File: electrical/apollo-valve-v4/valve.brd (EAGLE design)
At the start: 160 x 100 mm, 80 parts, among them J1 VALVE2, J2 VALVE1, J4 S1, J5 S2, U1 DRV8806-SSOP, U2 DRV8806-SSOP, U3 TPS54202, U4 DRV8806-SSOP, U5 DRV8806-SSOP, U6 TPS54202

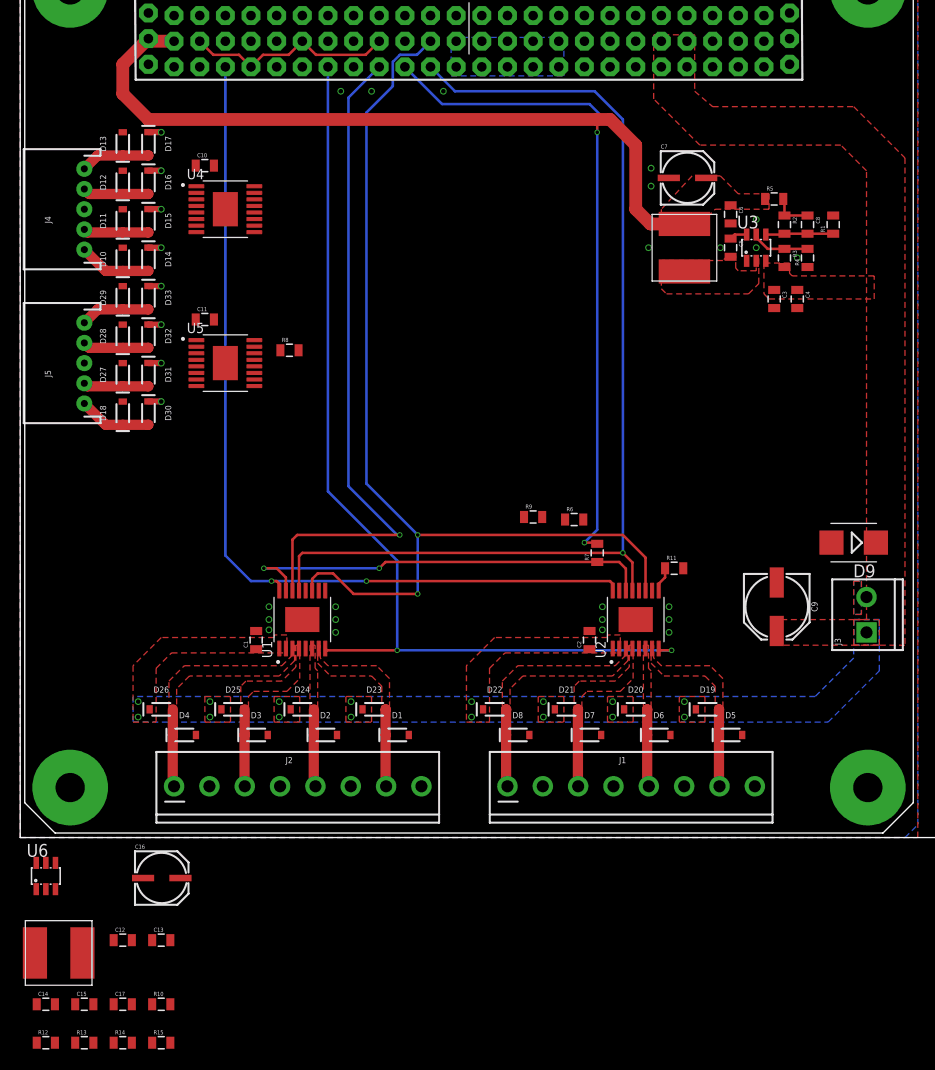
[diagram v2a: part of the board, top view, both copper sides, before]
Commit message: First layout pass for complete valve board
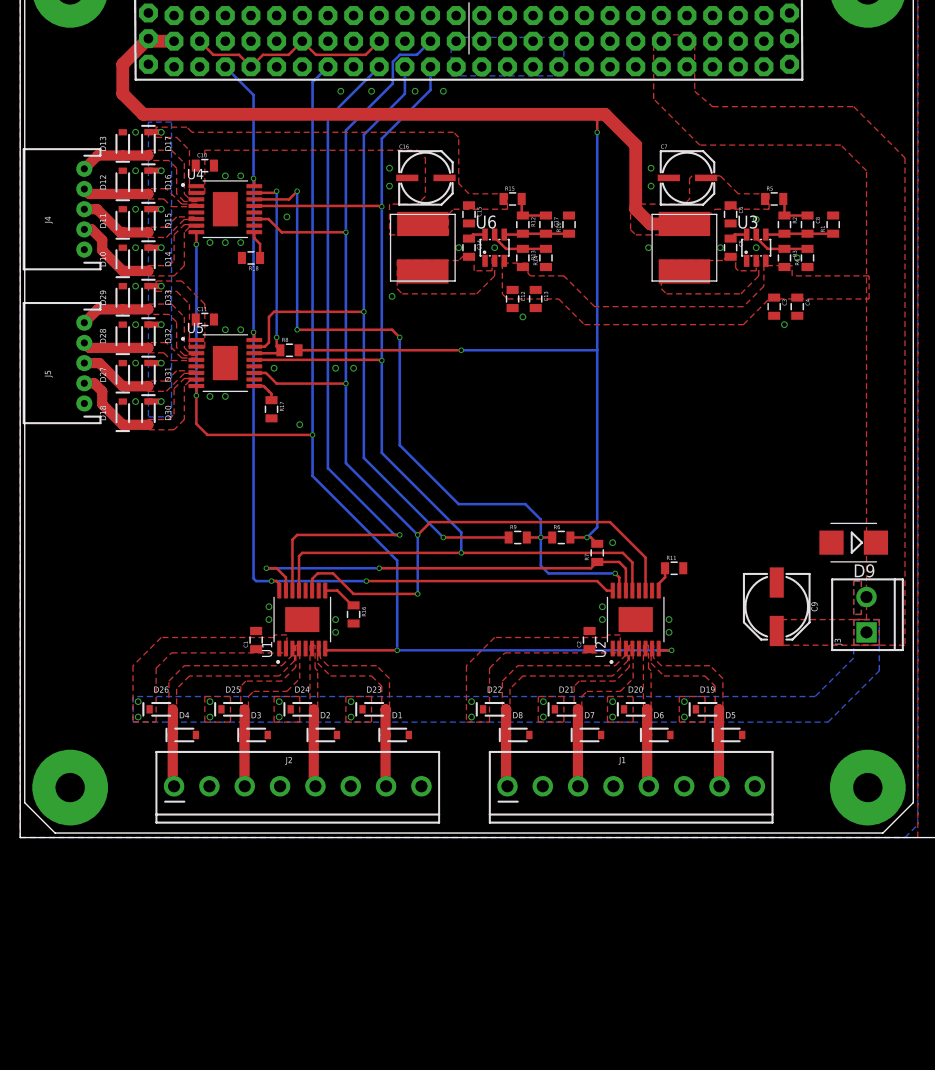
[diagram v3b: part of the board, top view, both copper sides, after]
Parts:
- added R16, R17, R18: 2.2K, apollo-ctrl-v4:0805
- moved R12 93.8 mm to (49.8, 60.7), turned to 270 degrees
- moved R15 90.5 mm to (48.8, 63.2)
- moved R13 89.0 mm to (49.8, 57.4), turned to 270 degrees
- moved R14 88.3 mm to (52.1, 57.4), turned to 90 degrees
- moved C17 87.9 mm to (52.1, 60.7), turned to 270 degrees
- moved R10 87.1 mm to (54.4, 60.7), turned to 90 degrees
- moved C15 87.0 mm to (44.5, 61.7), turned to 270 degrees
- moved C14 85.9 mm to (44.5, 58.4), turned to 270 degrees
- moved L2 78.6 mm to (39.9, 58.4), turned to 90 degrees
- moved U6 76.5 mm to (47.0, 58.4)
- moved C12 74.3 mm to (48.8, 53.3), turned to 270 degrees
- moved C16 74.1 mm to (40.1, 65.5)
- moved C13 73.5 mm to (51.1, 53.3), turned to 270 degrees
- moved R9 2.54 mm to (49.3, 29.7)
- moved R6 2.18 mm to (53.6, 29.7)
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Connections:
- removed net RESET: R11.1, U1.9, U2.9, U4.9, U5.9
- new net R1: R11.1, U2.9
- new net R2: R16.1, U1.9
- new net R3: R17.1, U5.9
- new net R4: R18.1, U4.9
- net GND: now also J4.1, J5.1, R16.2, R17.2, R18.2; no longer J4.3, J5.3
- net S1C: now also J4.3; no longer J4.2
- net S1D: now also J4.2; no longer J4.1
- net S2C: now also J5.3; no longer J5.2
- net S2D: now also J5.2; no longer J5.1
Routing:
- net CIDO2: track 0.00 -> 73.1 mm, vias 0 -> 5
- net CIDO: track 22.7 -> 71.8 mm, vias 0 -> 2
- net !LOE!: track 96.4 -> 129.5 mm, vias 2 -> 5
- net +5V: track 117.6 -> 148.7 mm, vias 2 -> 3
- net CS1: track 99.9 -> 121.8 mm, vias 2 -> 4
- net CIDO3: track 0.00 -> 20.9 mm, vias 0 -> 2
- net SCK: track 103.9 -> 118.4 mm, vias 1 -> 3
- net FB2: track 0.00 -> 6.45 mm
- net VEN2: track 0.00 -> 5.83 mm
- net FF2: track 0.00 -> 3.97 mm
- net R2: track 0.00 -> 3.41 mm
- net R4: track 0.00 -> 2.79 mm
- net R3: track 0.00 -> 2.65 mm
- net RESET: track 2.47 -> 0.00 mm
- net R1: track 0.00 -> 2.47 mm
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- added copper zone on layer 1, net +12V
- added copper zone on layer 16, net +12V
- added copper zone on layer 1, net S1A
- added copper zone on layer 1, net S1B
- added copper zone on layer 1, net S1C
- added copper zone on layer 1, net S1D
- added copper zone on layer 1, net S2A
- added copper zone on layer 1, net S2B
- added copper zone on layer 1, net S2C
- added copper zone on layer 1, net S2D
- added copper zone on layer 1, net SW2

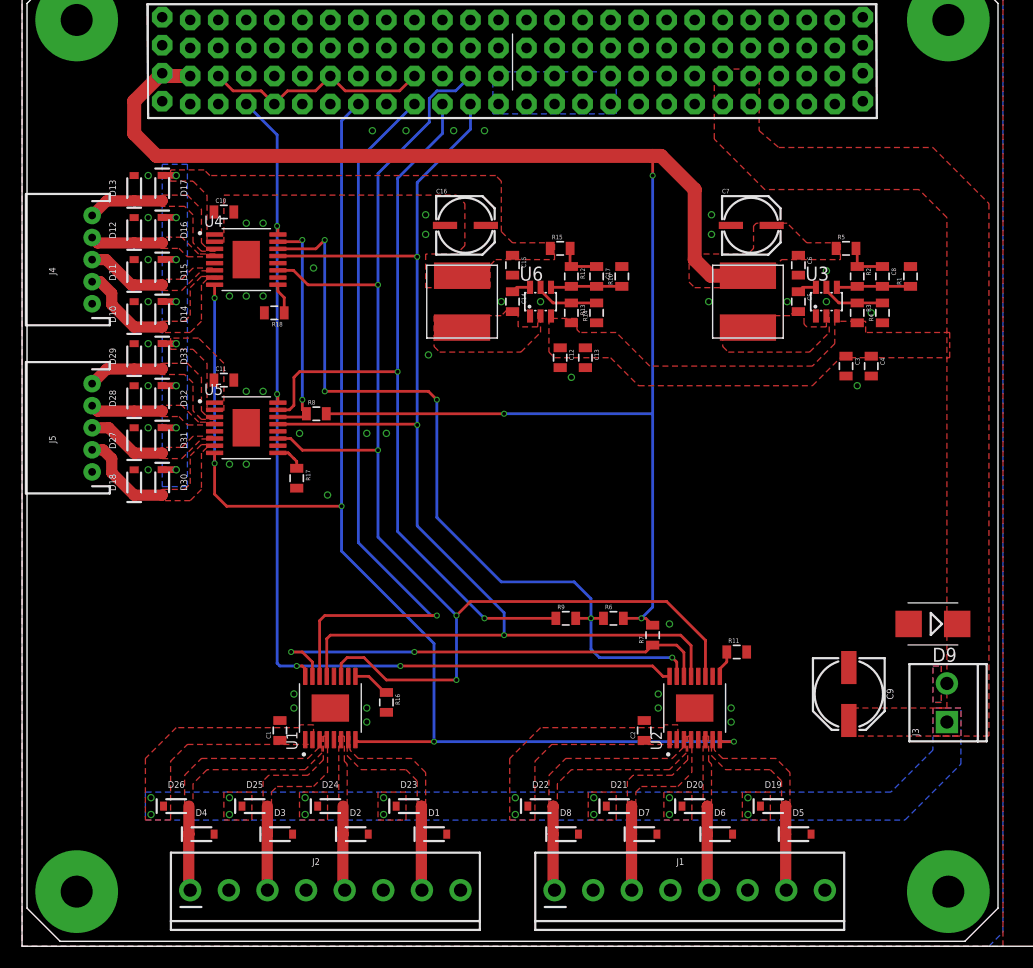
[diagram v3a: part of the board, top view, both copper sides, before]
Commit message: Clean up valve board silkscreen and change diodes to SOD-123
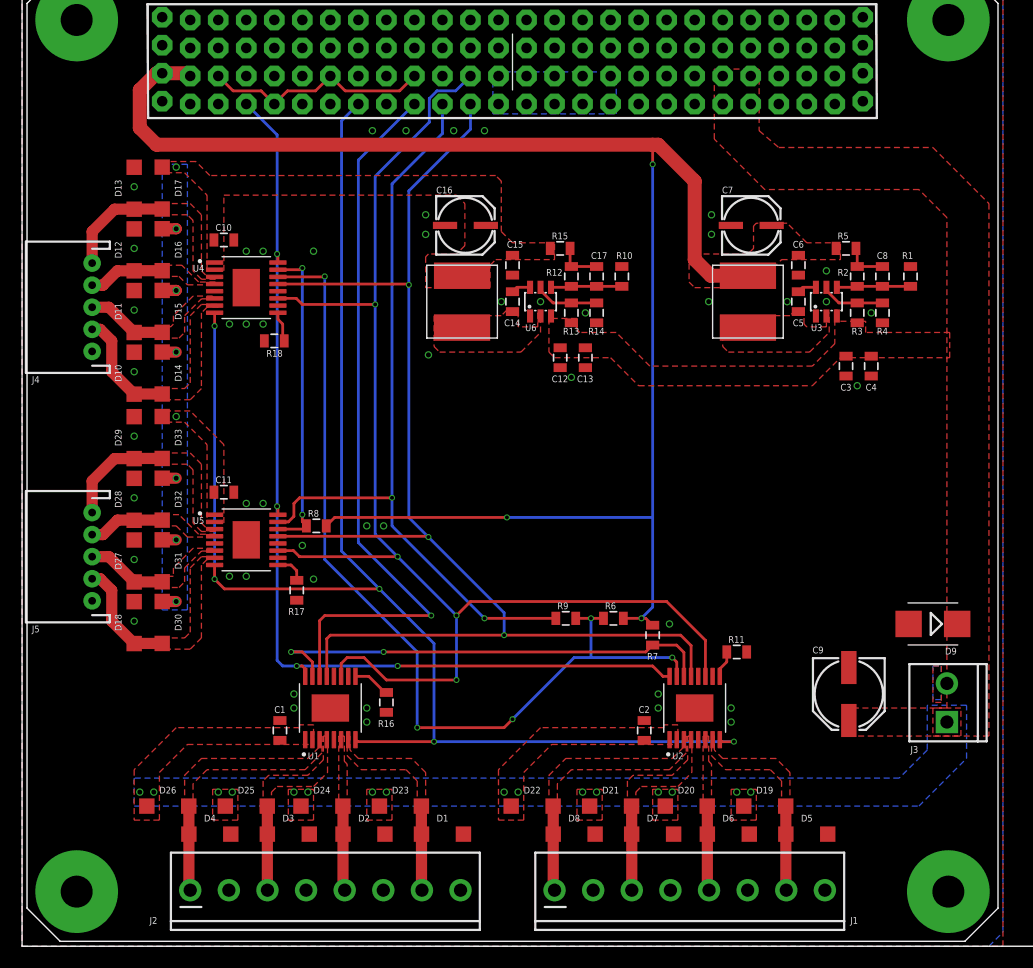
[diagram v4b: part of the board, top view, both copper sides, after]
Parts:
- D1, D10, D11, D12, D13, D14, D15, D16, D17, D18, D19, D2, D20, D21, D22, D23, D24, D25, D26, D27, D28, D29, D3, D30, D31, D32, D33, D4, D5, D6, D7, D8: value BAT46 -> B5819W; device SparkFun-DiscreteSemi:SOD-323 -> diode:SOD123
- moved D18 12.7 mm to (10.2, 29.3)
- moved D30 12.7 mm to (12.7, 29.3)
- moved J5 11.7 mm to (6.35, 35.3)
- moved D27 10.9 mm to (10.2, 34.9)
- moved D31 10.9 mm to (12.7, 34.9)
- moved U5 10.2 mm to (20.3, 36.8)
- moved C11 10.2 mm to (18.3, 41.1)
- moved R17 10.2 mm to (24.9, 32.3)
- moved R8 10.2 mm to (26.7, 38.1)
- moved D28 9.14 mm to (10.2, 40.5)
- moved D32 9.14 mm to (12.7, 40.5)
- moved D29 7.37 mm to (10.2, 46.1)
- moved D33 7.37 mm to (12.7, 46.1)
- moved D10 5.33 mm to (10.2, 51.9)
- moved D14 5.33 mm to (12.7, 52.0)
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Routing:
- net CIDO2: track 73.1 -> 82.3 mm
- net !LOE!: track 129.5 -> 138.3 mm
- net CIDO3: track 20.9 -> 28.5 mm
- net S2A: track 6.90 -> 10.1 mm
- net S1A: track 6.90 -> 10.1 mm
- net +12V: track 10.2 -> 7.63 mm
- net S1D: track 8.66 -> 10.4 mm
- net S2D: track 8.81 -> 10.4 mm
- net CIDO: track 71.8 -> 70.4 mm
- net CS1: track 121.8 -> 123.0 mm
- net +5V: track 148.7 -> 149.7 mm
- net CODI: track 67.6 -> 66.6 mm
- net SCK: track 118.4 -> 119.3 mm
- net GND: vias 49 -> 50
